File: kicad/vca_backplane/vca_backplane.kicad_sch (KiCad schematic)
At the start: 27 parts, among them J1 Conn_02x20_Odd_Even, J11 Conn_01x03, J2 Eurorack Power, Q1 DMMT5401, Q2 DMG2305UX, U1 74HCT138, U11 74HCT138, U8 M24C02-WMN

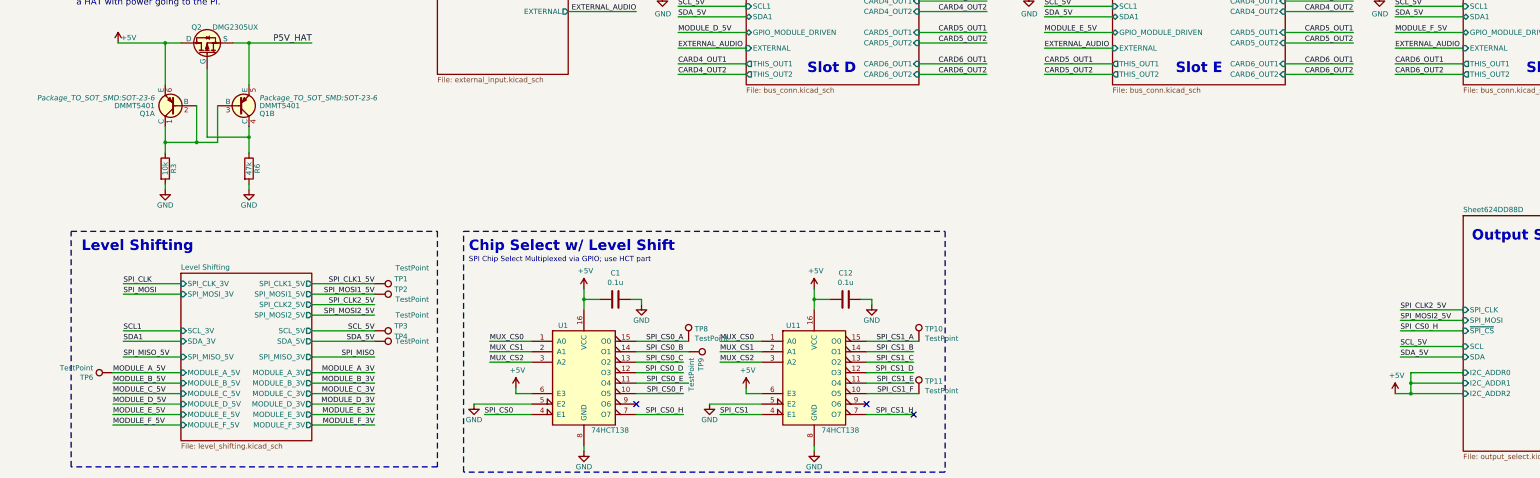
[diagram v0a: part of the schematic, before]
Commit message: add external input sheet.  Basic routing on backplane done- needs cleaning up
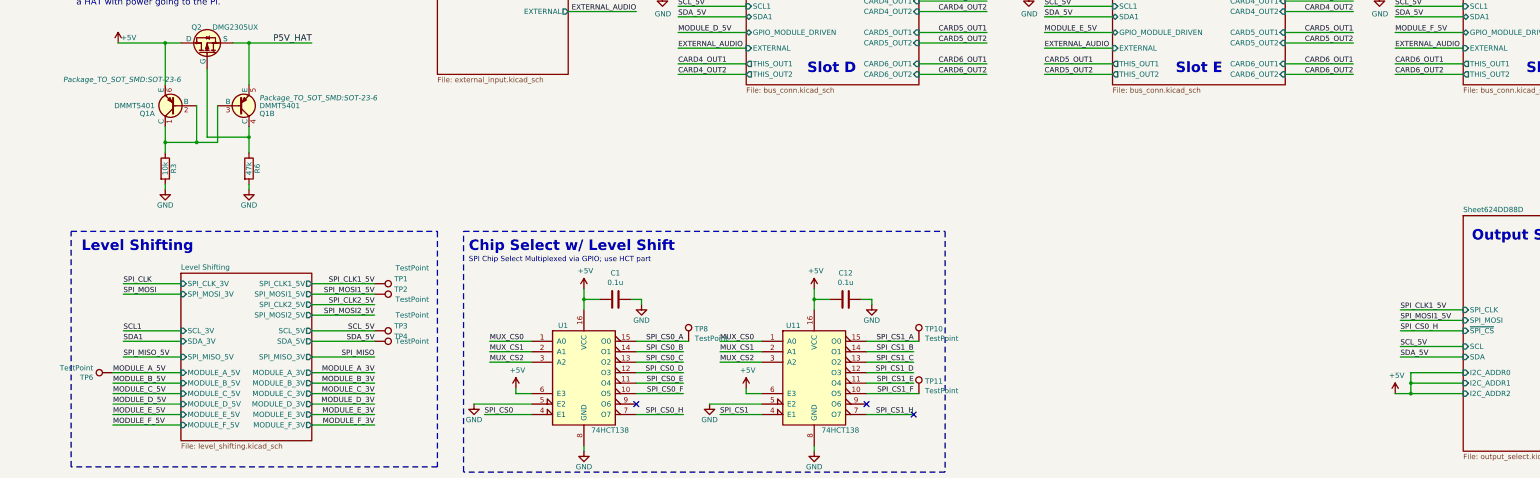
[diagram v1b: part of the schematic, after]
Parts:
- removed TP9: TestPoint, TestPoint:TestPoint_Pad_2.0x2.0mm, symbol Connector:TestPoint
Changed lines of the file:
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@@
     (stroke (width 0) (type default))
   )
+  (wire (pts (xy 154.94 191.77) (xy 166.37 191.77))
+    (stroke (width 0) (type default))
+  )
   (wire (pts (xy 271.78 60.96) (xy 255.27 60.96))
     (stroke (width 0) (type default))
@@
     (stroke (width 0) (type default))
   )
-  (wire (pts (xy 154.94 184.15) (xy 167.64 184.15))
-    (stroke (width 0) (type default))
-  )
   (wire (pts (xy 119.38 240.03) (xy 121.92 240.03))
     (stroke (width 0) (type default))
@@
     (stroke (width 0) (type default))
   )
-  (wire (pts (xy 154.94 191.77) (xy 167.64 191.77))
-    (stroke (width 0) (type default))
-  )
   (wire (pts (xy 76.2 189.23) (xy 91.44 189.23))
     (stroke (width 0) (type default))
@@
     (stroke (width 0) (type default))
   )
+  (wire (pts (xy 154.94 184.15) (xy 166.37 184.15))
+    (stroke (width 0) (type default))
+  )
   (text "5V Powered HAT Protection" (at 25.4 92.71 0)
     (effects (font (size 2.9972 2.9972) (thickness 0.5994) bold) (justify left bottom))
@@
     (effects (font (size 1.27 1.27)) (justify right bottom))
   )
-  (label "SPI_CLK2_5V" (at 340.36 173.99 0) (fields_autoplaced)
+  (label "SPI_CLK1_5V" (at 340.36 173.99 0) (fields_autoplaced)
     (effects (font (size 1.27 1.27)) (justify left bottom))
   )
@@
     (effects (font (size 1.27 1.27)) (justify left bottom))
   )
-  (label "SPI_MOSI2_5V" (at 340.36 176.53 0) (fields_autoplaced)
+  (label "SPI_MOSI1_5V" (at 340.36 176.53 0) (fields_autoplaced)
     (effects (font (size 1.27 1.27)) (justify left bottom))
   )
@@
       (effects (font (size 1.27 1.27)) (justify left))
     )
-    (property "Footprint" "Package_TO_SOT_SMD:SOT-23-6" (at 38.1 122.555 0)
+    (property "Footprint" "Package_TO_SOT_SMD:SOT-23-6" (at 44.45 118.11 0)
       (effects (font (size 1.27 1.27) italic) (justify left))
     )
@@
         )
       )
-    )
-  )
-  (symbol (lib_id "Connector:TestPoint") (at 167.64 184.15 270) (unit 1)
-    (in_bom yes) (on_board yes) (dnp no)
-    (property "Reference" "TP9" (at 170.6372 185.6232 0)
-      (effects (font (size 1.27 1.27)) (justify left))
-    )
-    (property "Value" "TestPoint" (at 168.3258 185.6232 0)
-      (effects (font (size 1.27 1.27)) (justify left))
-    )
-    (property "Footprint" "TestPoint:TestPoint_Pad_2.0x2.0mm" (at 167.64 189.23 0)
-      (effects (font (size 1.27 1.27)) hide)
-    )
-    (property "Datasheet" "~" (at 167.64 189.23 0)
-      (effects (font (size 1.27 1.27)) hide)
-    )
-    (property "Digikey" "952-2664-2-ND" (at 167.64 184.15 0)
-      (effects (font (size 1.27 1.27)) hide)
-    )
-    (pin "1")
-    (instances
-      (project "vca_backplane"
-        (path "/bdbd6910-8f28-459f-89ba-e6dd447d59a9"
-          (reference "TP9") (unit 1)
-        )
-      )

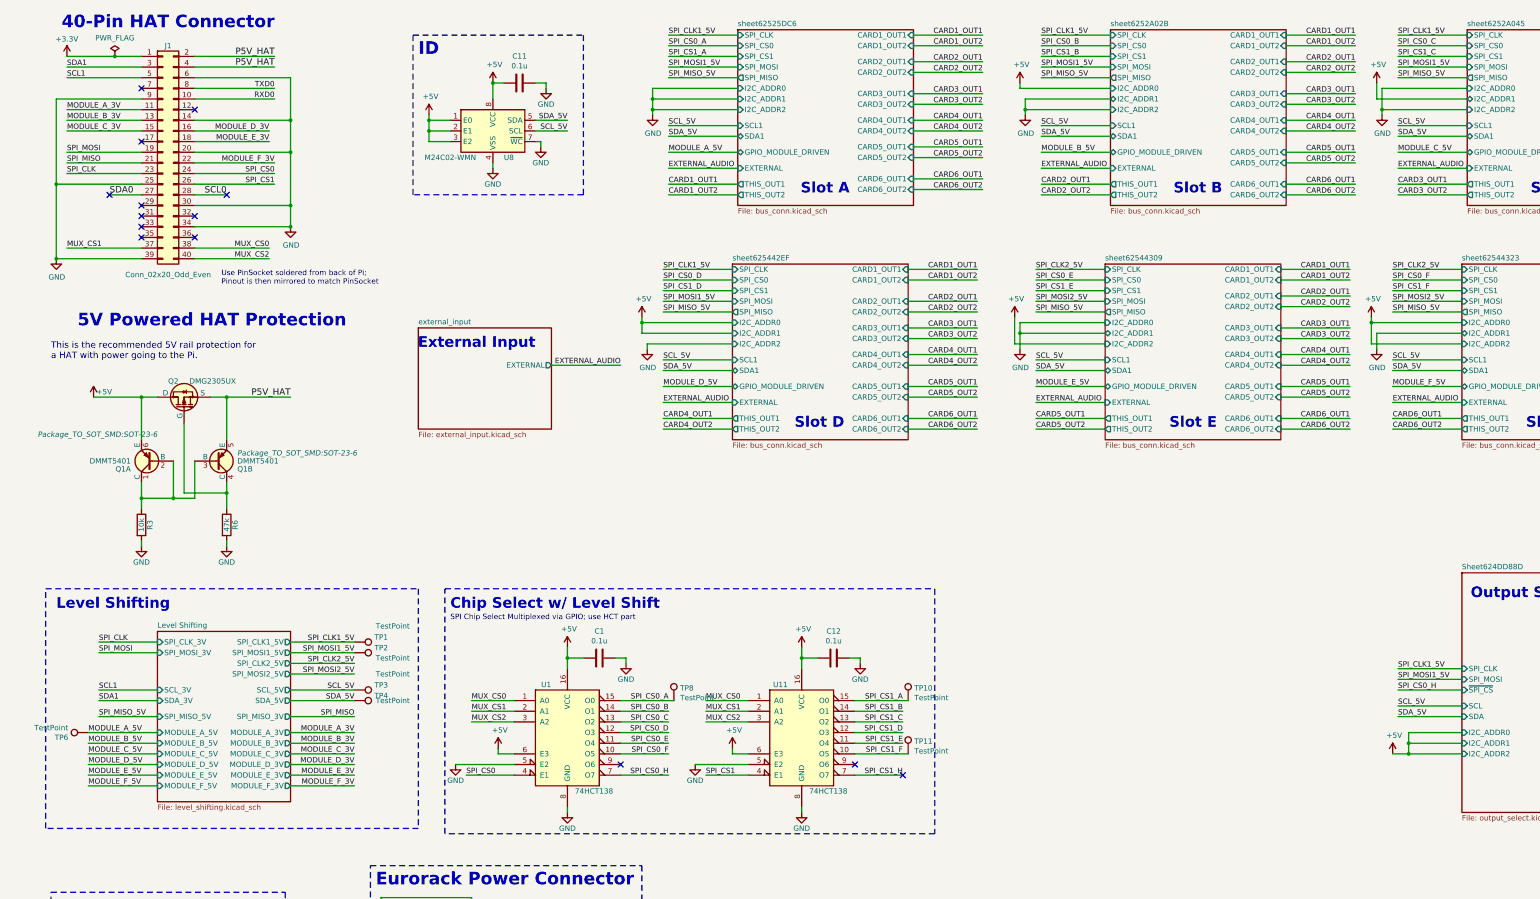
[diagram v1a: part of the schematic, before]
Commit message: use additional buffer for spi clock/mosi
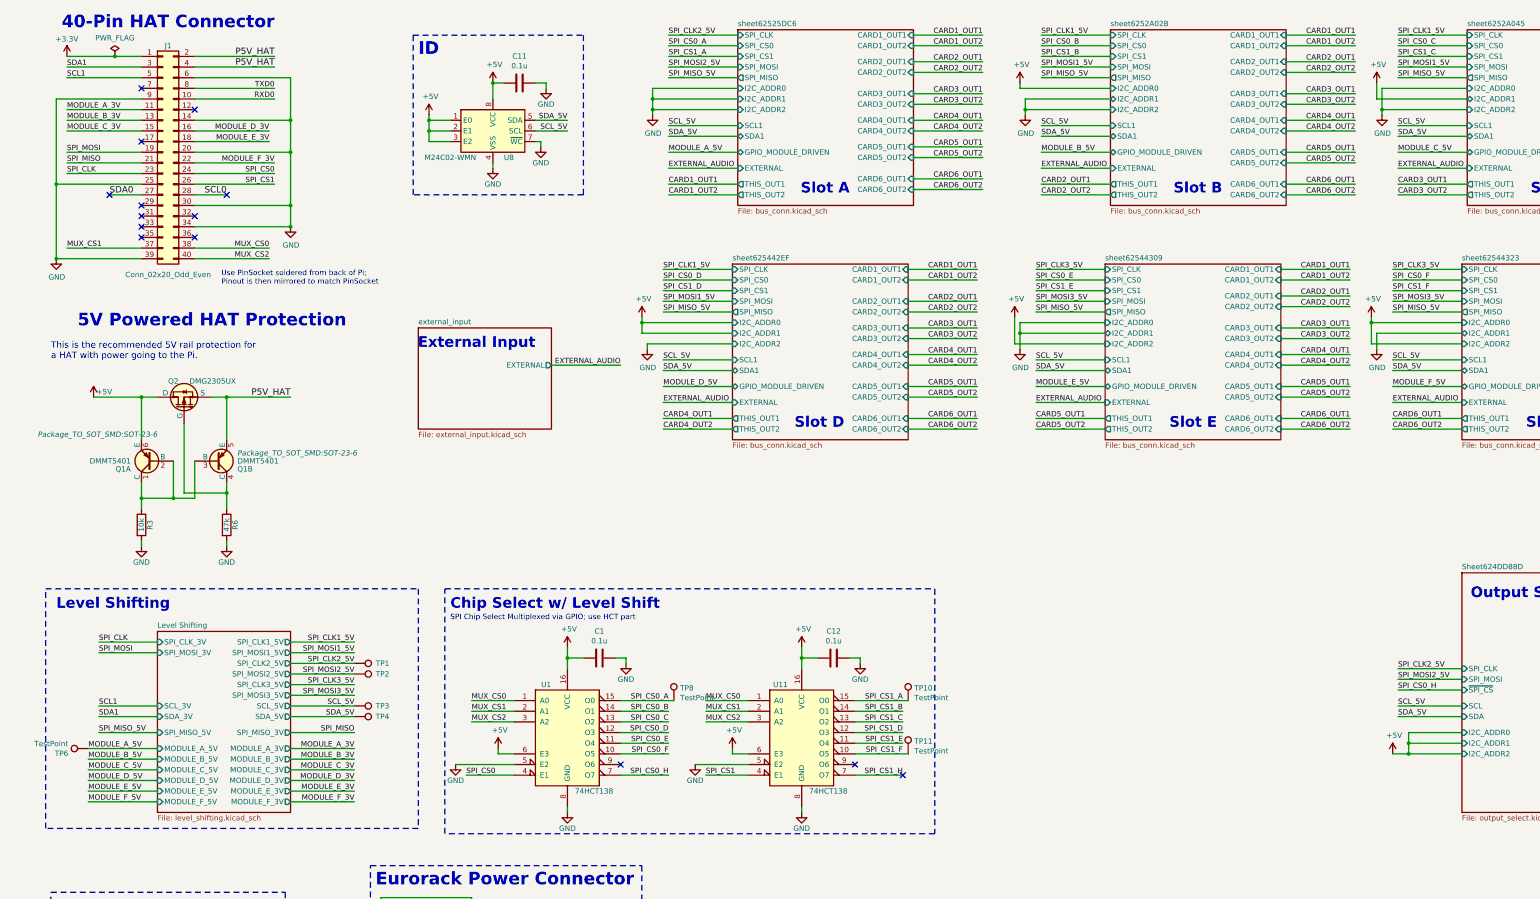
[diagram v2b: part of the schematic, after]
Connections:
- net SPI_CLK1_5V: no longer TP1.1
- net SPI_CLK2_5V: now also TP1.1
- net SPI_MOSI1_5V: no longer TP2.1
- net SPI_MOSI2_5V: now also TP2.1
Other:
- sheet Level Shifting ports: added SPI_CLK3_5V, SPI_MOSI3_5V; removed none
- moved on the sheet: TP1, TP2, TP3, TP4, TP6

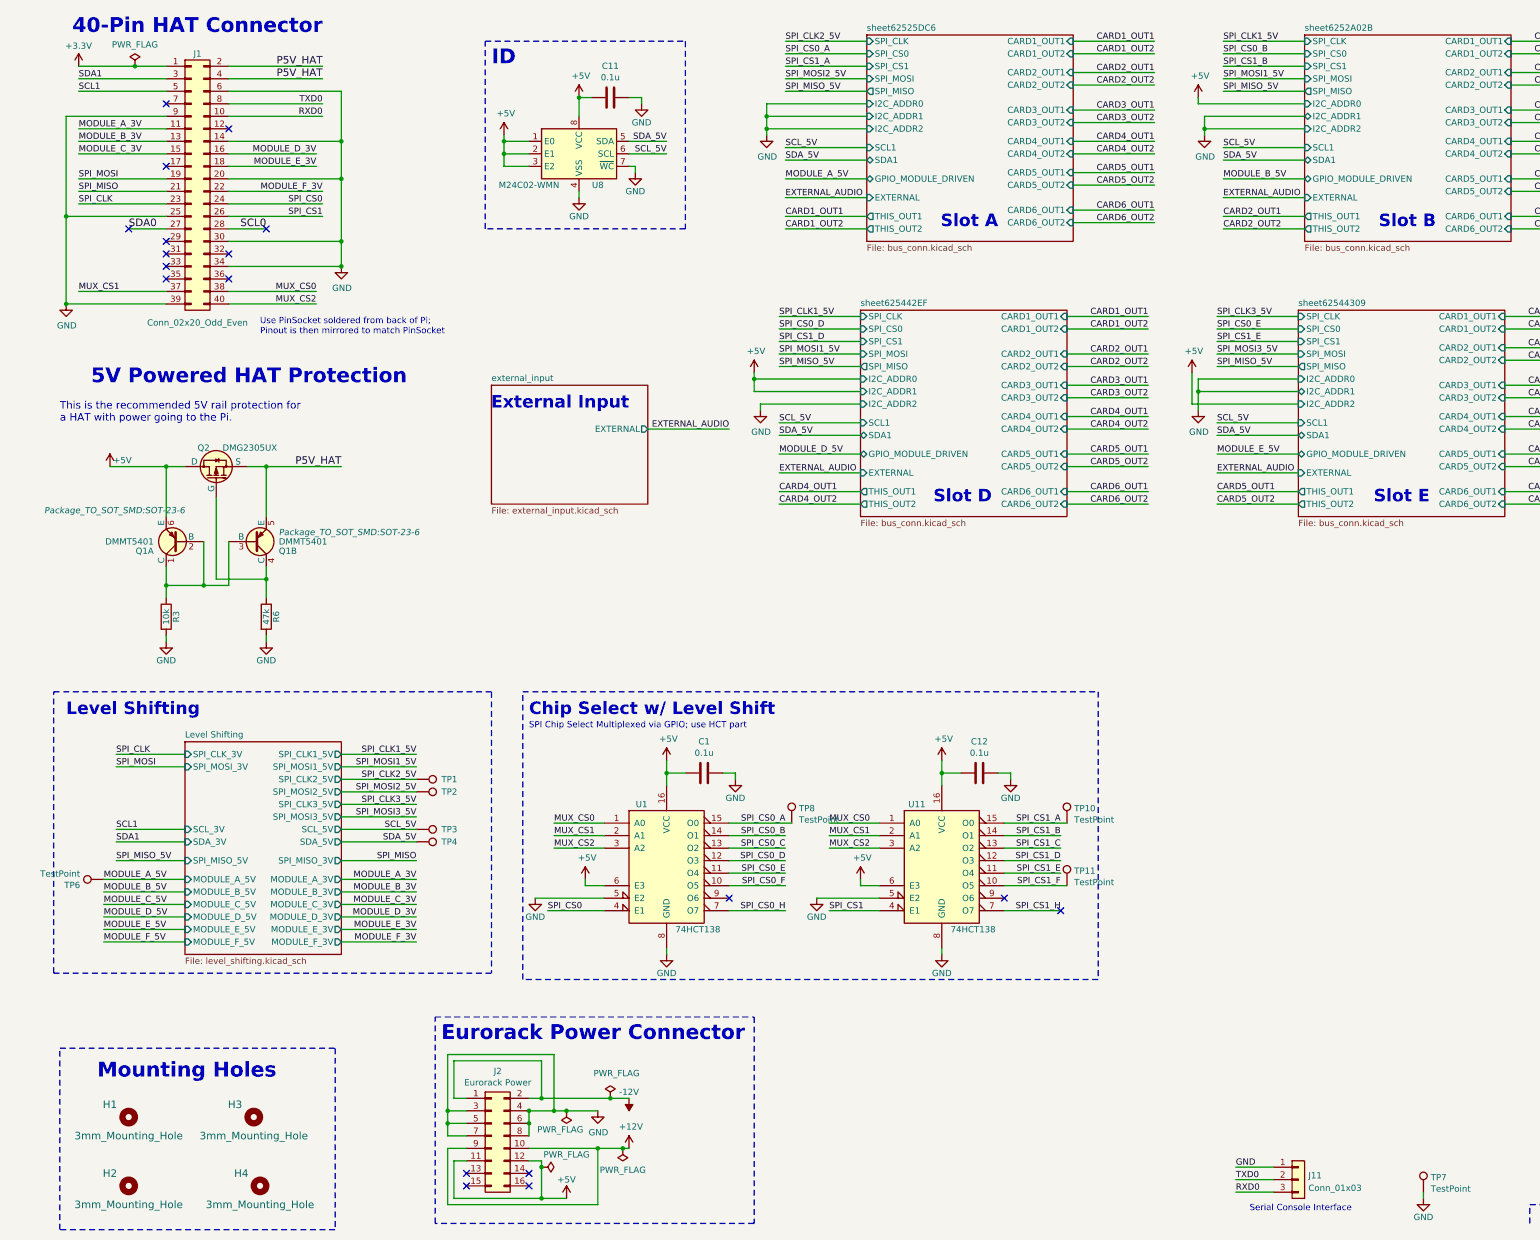
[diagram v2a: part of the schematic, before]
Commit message: geographically reorientated from pcb
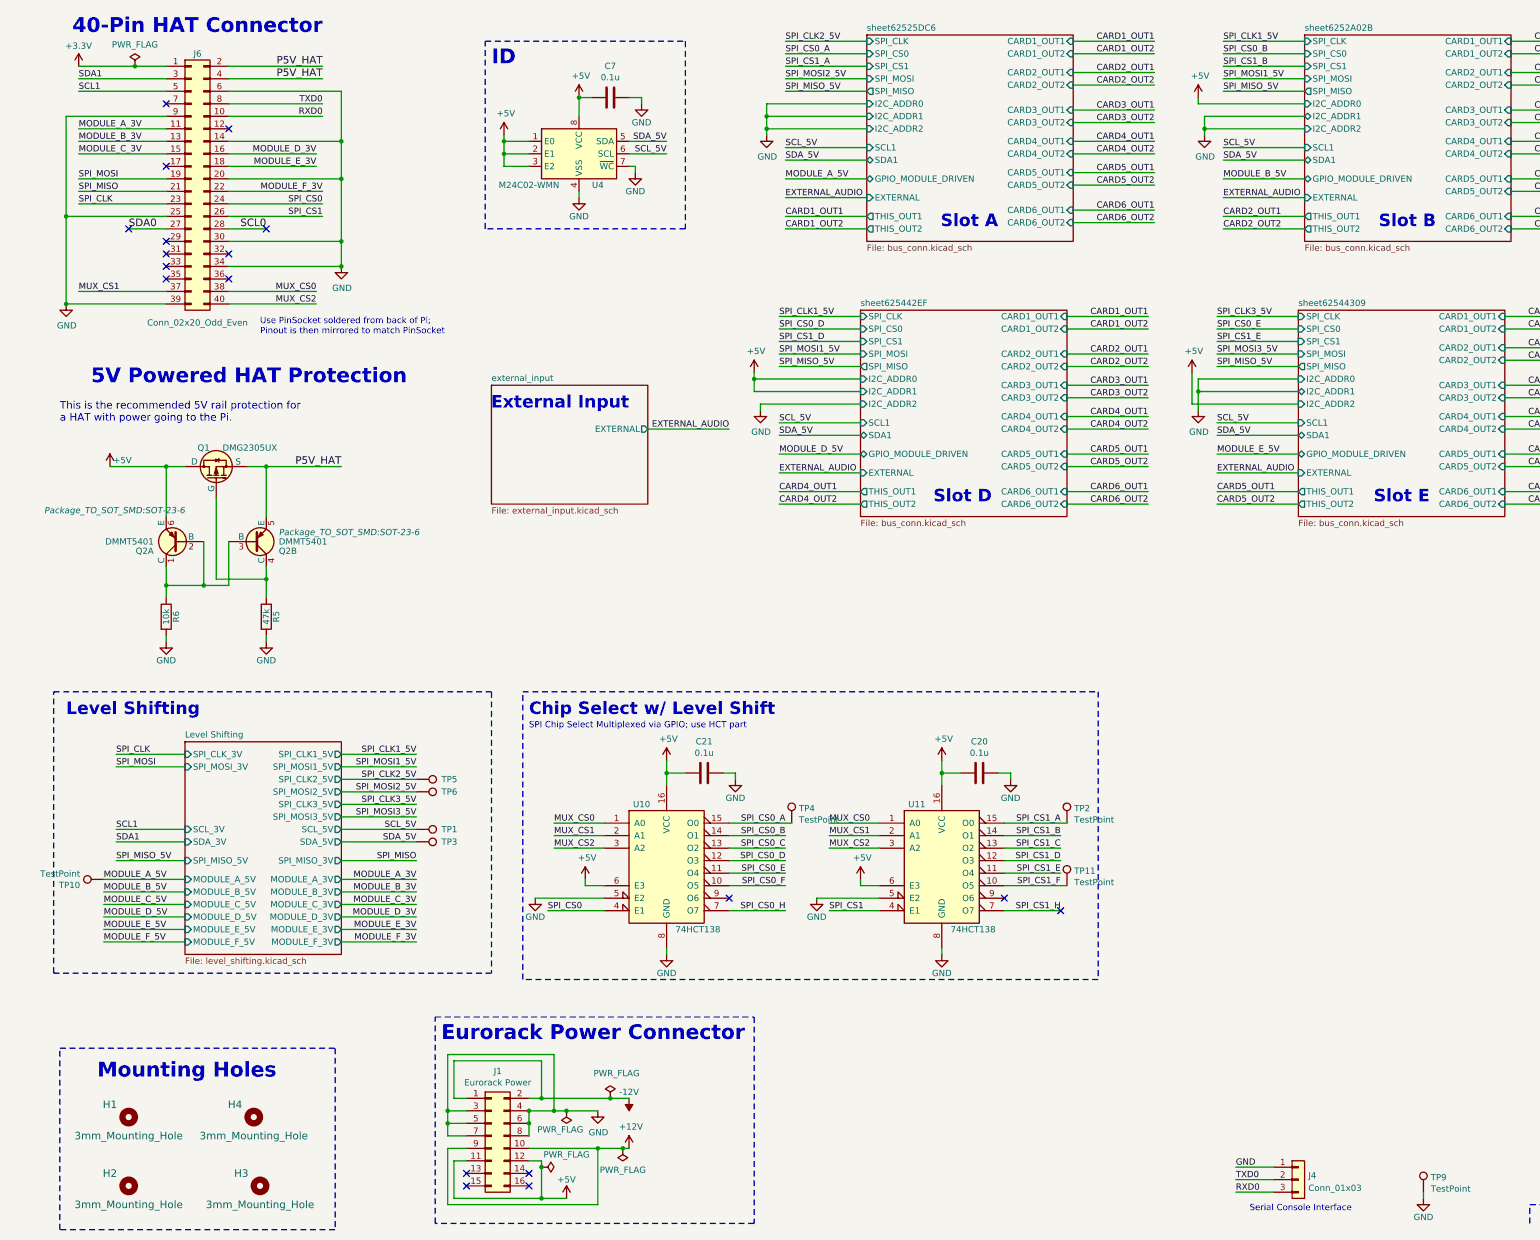
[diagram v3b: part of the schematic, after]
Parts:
- renumbered C12 to C20, C1 to C21, C11 to C7, H4 to H3, H3 to H4, J2 to J1, J11 to J4, J1 to J6, Q2 to Q1, Q1 to Q2, R6 to R5, R3 to R6, TP3 to TP1, TP6 to TP10, TP10 to TP2, TP4 to TP3, TP8 to TP4, TP1 to TP5, TP2 to TP6, TP7 to TP9, U1 to U10, U8 to U4
